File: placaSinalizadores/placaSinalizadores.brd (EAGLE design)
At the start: 41.9 x 27.9 mm, 10 parts

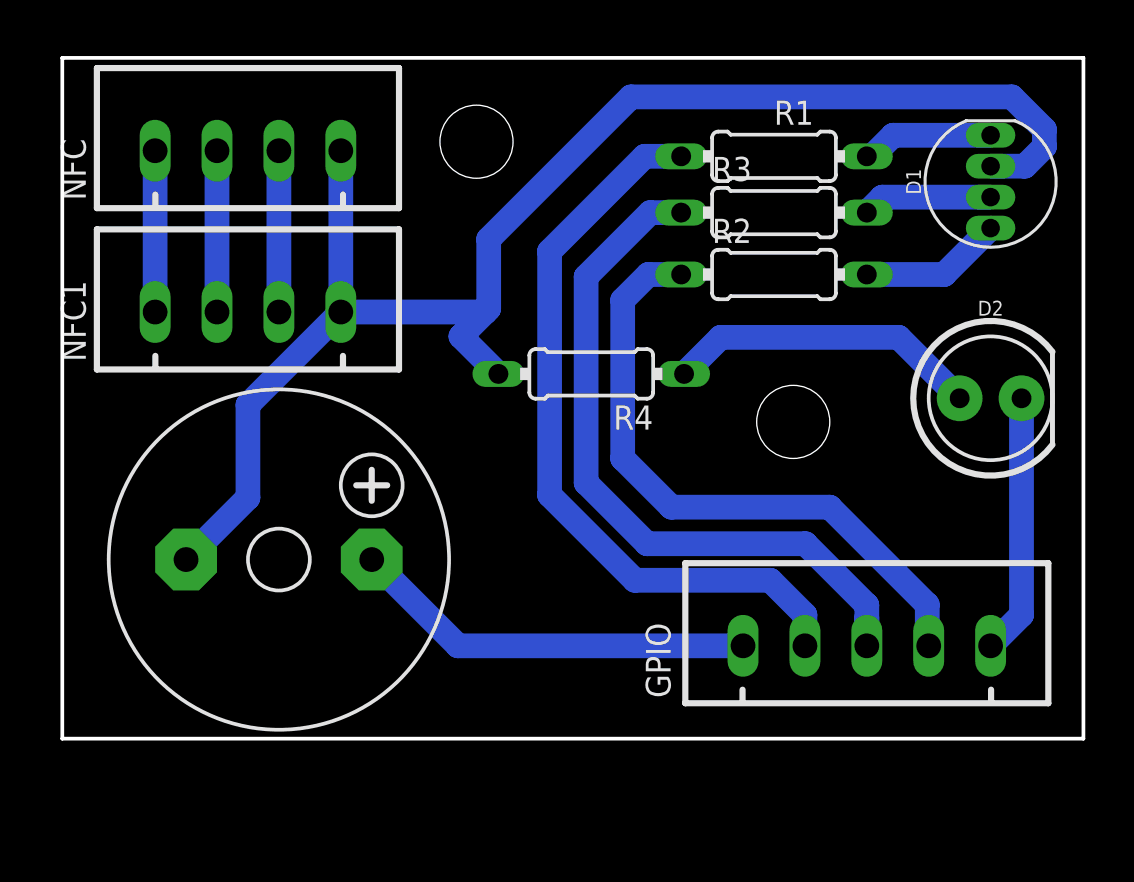
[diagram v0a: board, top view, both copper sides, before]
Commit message: placa de sinalização V2
placa com conectores para o reset adicionados e correção do erro para o led rgb
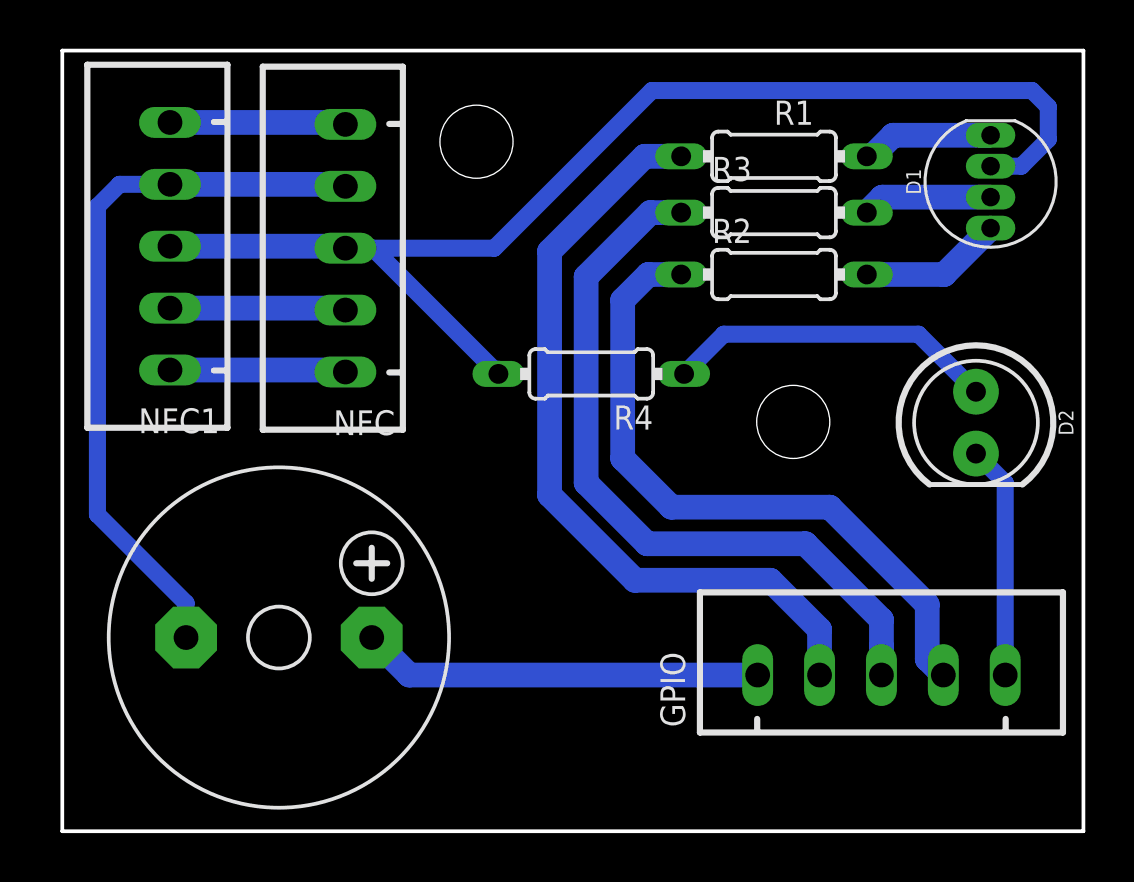
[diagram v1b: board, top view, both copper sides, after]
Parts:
- NFC, NFC1: device jst-xh-ornan:JST-XH-04-PACKAGE-LONG-PAD -> jst-xh-ornan:JST-XH-05-PACKAGE-LONG-PAD
- moved NFC 5.66 mm to (11.6, 20.1), turned to 90 degrees
- moved NFC1 4.19 mm to (4.42, 20.2), turned to 90 degrees
- moved SG2 3.20 mm to (8.89, 4.15)
- moved GPIO 1.34 mm to (33.6, 2.61)
- moved D2 1.17 mm to (37.5, 13.0), turned to 270 degrees
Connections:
- new net N$12: NFC.5, NFC1.5
- net GND: no longer D1.2, R4.2
- net VCC: now also D1.2, R4.2
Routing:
- net VCC: track 6.62 -> 51.6 mm
- net GND: track 61.0 -> 29.8 mm
- net N$12: track 0.00 -> 7.23 mm
- net N$9: track 30.8 -> 32.3 mm
- net N$11: track 29.9 -> 31.3 mm
- net N$10: track 26.0 -> 27.5 mm
- net N$7: track 10.7 -> 9.59 mm
- net N$4: track 13.0 -> 13.6 mm
- net N$5: track 6.62 -> 7.23 mm
- net N$6: track 6.62 -> 7.23 mm
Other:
- board size 41.9 x 27.9 mm -> 41.9 x 32 mm
